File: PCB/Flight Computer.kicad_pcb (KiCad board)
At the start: 6 copper layers, 30 x 60 mm, 80 parts, among them J501 Conn_02x03_Counter_Clockwise, J502 USB_C_Receptacle_USB2.0_16P, J503 Screw_Terminal_01x06, J504 Screw_Terminal_01x04, J505 Conn_01x04, J506 Conn_02x03_Counter_Clockwise, J507 Conn_01x05, J601 Conn_Coaxial, U201 LM1117MP-3.3, U301 W25Q128JVS, U302 STM32F446RETx, U401 MMC5633NJL, U402 LSM6DSV320, U403 MS5607-02BA, U404 SAM-M8Q, U601 RFM95W-915S2, Y301 Resonator

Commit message: Renamed nets from pryo to pyro cause I can't spell
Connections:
- net /Pryo1 renamed /Pyro1
- net /Pryo1_Cont renamed /Pyro1_Cont
- net /Pryo1_Trigger renamed /Pyro1_Trigger
- net /Pryo2 renamed /Pyro2
- net /Pryo2_Cont renamed /Pyro2_Cont
- net /Pryo2_Trigger renamed /Pyro2_Trigger
- net /Pryo3 renamed /Pyro3
- net /Pryo3_Cont renamed /Pyro3_Cont
- net /Pryo3_Trigger renamed /Pyro3_Trigger
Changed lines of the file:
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@@
 	(net 11 "/NRST")
 	(net 12 "/SWCLK")
-	(net 13 "/Pryo3")
+	(net 13 "/Pyro3")
 	(net 14 "/USB_DP_N")
 	(net 15 "/USB_DP_P")
 	(net 16 "Pyro_Power")
-	(net 17 "/Pryo1")
-	(net 18 "/Pryo2")
+	(net 17 "/Pyro1")
+	(net 18 "/Pyro2")
 	(net 19 "/I2C_SDA")
 	(net 20 "/I2C_SCL")
@@
 	(net 28 "/Servo1")
 	(net 29 "Net-(J601-In)")
-	(net 30 "/Pryo1_Cont")
-	(net 31 "/Pryo2_Cont")
-	(net 32 "/Pryo3_Cont")
+	(net 30 "/Pyro1_Cont")
+	(net 31 "/Pyro2_Cont")
+	(net 32 "/Pyro3_Cont")
 	(net 33 "/MCU/OSC_OUT")
 	(net 34 "/{slash}GPS_RESET")
@@
 	(net 37 "/Armed")
 	(net 38 "Net-(U701A-G)")
-	(net 39 "/Pryo1_Trigger")
+	(net 39 "/Pyro1_Trigger")
 	(net 40 "Net-(U702B-G)")
-	(net 41 "/Pryo2_Trigger")
+	(net 41 "/Pyro2_Trigger")
 	(net 42 "Net-(U702A-G)")
 	(net 43 "Net-(U703B-G)")
 	(net 44 "Net-(U703A-G)")
-	(net 45 "/Pryo3_Trigger")
+	(net 45 "/Pyro3_Trigger")
 	(net 46 "/MCU/FLASH_CS")
 	(net 47 "/MCU/{slash}FLASH_WP")
@@
 			(layers "F.Cu" "F.Mask" "F.Paste")
 			(roundrect_rratio 0.25)
-			(net 31 "/Pryo2_Cont")
+			(net 31 "/Pyro2_Cont")
 			(pintype "passive")
 		)
@@
 			(layers "*.Cu" "*.Mask")
 			(remove_unused_layers no)
-			(net 13 "/Pryo3")
+			(net 13 "/Pyro3")
 			(pinfunction "Pin_2")
 			(pintype "passive")
@@
 			(layers "F.Cu" "F.Mask" "F.Paste")
 			(roundrect_rratio 0.25)
-			(net 41 "/Pryo2_Trigger")
+			(net 41 "/Pyro2_Trigger")
 			(pintype "passive")
 		)
@@
 			(size 0.2992 0.6298)
 			(layers "F.Cu" "F.Mask" "F.Paste")
-			(net 18 "/Pryo2")
+			(net 18 "/Pyro2")
 			(pinfunction "D")
 			(pintype "passive")
@@
 			(size 0.9906 0.7112)
 			(layers "F.Cu" "F.Mask" "F.Paste")
-			(net 18 "/Pryo2")
+			(net 18 "/Pyro2")
 			(pinfunction "D")
 			(pintype "passive")
@@
 			(layers "*.Cu" "*.Mask")
 			(remove_unused_layers no)
-			(net 17 "/Pryo1")
+			(net 17 "/Pyro1")
 			(pinfunction "Pin_3")
 			(pintype "passive")
@@
 			(layers "*.Cu" "*.Mask")
 			(remove_unused_layers no)
-			(net 18 "/Pryo2")
+			(net 18 "/Pyro2")
 			(pinfunction "Pin_5")
 			(pintype "passive")
@@
 			(layers "F.Cu" "F.Mask" "F.Paste")
 			(roundrect_rratio 0.25)
-			(net 31 "/Pryo2_Cont")
+			(net 31 "/Pyro2_Cont")
 			(pintype "passive")
 		)
@@
 			(size 0.2992 0.6298)
 			(layers "B.Cu" "B.Mask" "B.Paste")
-			(net 17 "/Pryo1")
+			(net 17 "/Pyro1")
 			(pinfunction "D")
 			(pintype "passive")
@@
 			(size 0.9906 0.7112)
 			(layers "B.Cu" "B.Mask" "B.Paste")
-			(net 17 "/Pryo1")
+			(net 17 "/Pyro1")
 			(pinfunction "D")
 			(pintype "passive")
@@
 			(layers "B.Cu" "B.Mask" "B.Paste")
 			(roundrect_rratio 0.25)
-			(net 32 "/Pryo3_Cont")
+			(net 32 "/Pyro3_Cont")
 			(pintype "passive")
 		)
@@
 			(layers "B.Cu" "B.Mask" "B.Paste")
 			(roundrect_rratio 0.25)
-			(net 32 "/Pryo3_Cont")
+			(net 32 "/Pyro3_Cont")
 			(pintype "passive")
 		)
@@
 			(layers "B.Cu" "B.Mask" "B.Paste")
 			(roundrect_rratio 0.25)
-			(net 39 "/Pryo1_Trigger")
+			(net 39 "/Pyro1_Trigger")
 			(pintype "passive")
 		)
@@
 			(layers "B.Cu" "B.Mask" "B.Paste")
 			(roundrect_rratio 0.25)
-			(net 13 "/Pryo3")
+			(net 13 "/Pyro3")
 			(pintype "passive")
 		)
@@
 			(layers "B.Cu" "B.Mask" "B.Paste")
 			(roundrect_rratio 0.25)
-			(net 18 "/Pryo2")
+			(net 18 "/Pyro2")
 			(pintype "passive")
 		)
@@
 			(layers "B.Cu" "B.Mask" "B.Paste")
 			(roundrect_rratio 0.25)
-			(net 30 "/Pryo1_Cont")
+			(net 30 "/Pyro1_Cont")
 			(pintype "passive")
 		)
@@
 			(layers "B.Cu" "B.Mask" "B.Paste")
 			(roundrect_rratio 0.25)
-			(net 45 "/Pryo3_Trigger")
+			(net 45 "/Pyro3_Trigger")
 			(pintype "passive")
 		)
@@
 			(layers "B.Cu" "B.Mask" "B.Paste")
 			(roundrect_rratio 0.25)
-			(net 17 "/Pryo1")
+			(net 17 "/Pyro1")
 			(pintype "passive")
 		)
@@
 			(layers "B.Cu" "B.Mask" "B.Paste")
 			(roundrect_rratio 0.25)
-			(net 45 "/Pryo3_Trigger")
+			(net 45 "/Pyro3_Trigger")
 			(pinfunction "PC1")
 			(pintype "bidirectional")
@@
 			(layers "B.Cu" "B.Mask" "B.Paste")
 			(roundrect_rratio 0.25)
-			(net 41 "/Pryo2_Trigger")
+			(net 41 "/Pyro2_Trigger")
 			(pinfunction "PC2")
 			(pintype "bidirectional")
@@
 			(layers "B.Cu" "B.Mask" "B.Paste")
 			(roundrect_rratio 0.25)
-			(net 39 "/Pryo1_Trigger")
+			(net 39 "/Pyro1_Trigger")
 			(pinfunction "PC3")
 			(pintype "bidirectional")
@@
 			(layers "B.Cu" "B.Mask" "B.Paste")
 			(roundrect_rratio 0.25)
-			(net 31 "/Pryo2_Cont")
+			(net 31 "/Pyro2_Cont")
 			(pinfunction "PA0")
 			(pintype "bidirectional")
@@
 			(layers "B.Cu" "B.Mask" "B.Paste")
 			(roundrect_rratio 0.25)
-			(net 30 "/Pryo1_Cont")
+			(net 30 "/Pyro1_Cont")
 			(pinfunction "PA1")
 			(pintype "bidirectional")
@@
 			(layers "B.Cu" "B.Mask" "B.Paste")
 			(roundrect_rratio 0.25)
-			(net 32 "/Pryo3_Cont")
+			(net 32 "/Pyro3_Cont")
 			(pinfunction "PA3")
 			(pintype "bidirectional")
@@
 			(size 0.2992 0.6298)
 			(layers "B.Cu" "B.Mask" "B.Paste")
-			(net 13 "/Pryo3")
+			(net 13 "/Pyro3")
 			(pinfunction "D")
 			(pintype "passive")
@@
 			(size 0.9906 0.7112)
 			(layers "B.Cu" "B.Mask" "B.Paste")
-			(net 13 "/Pryo3")
+			(net 13 "/Pyro3")
 			(pinfunction "D")
 			(pintype "passive")
@@
 			(layers "B.Cu" "B.Mask" "B.Paste")
 			(roundrect_rratio 0.25)
-			(net 30 "/Pryo1_Cont")
+			(net 30 "/Pyro1_Cont")
 			(pintype "passive")
 		)

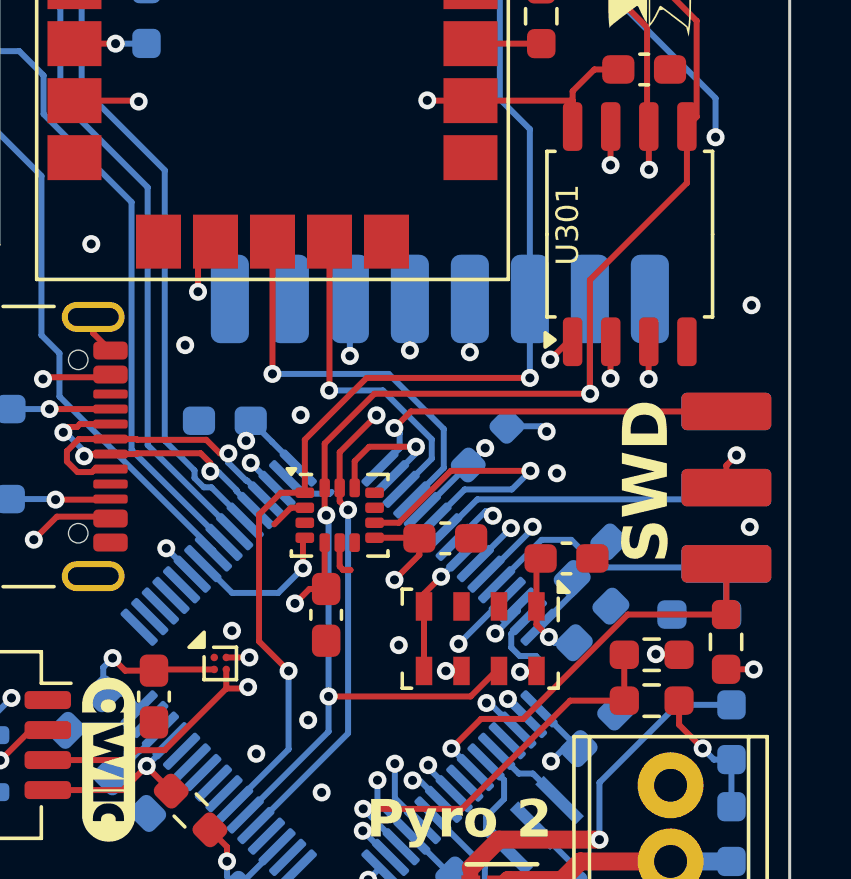
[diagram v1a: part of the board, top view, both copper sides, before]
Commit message: Flipped MOSI and MISO on the IMU
Updated all output files for the PCB
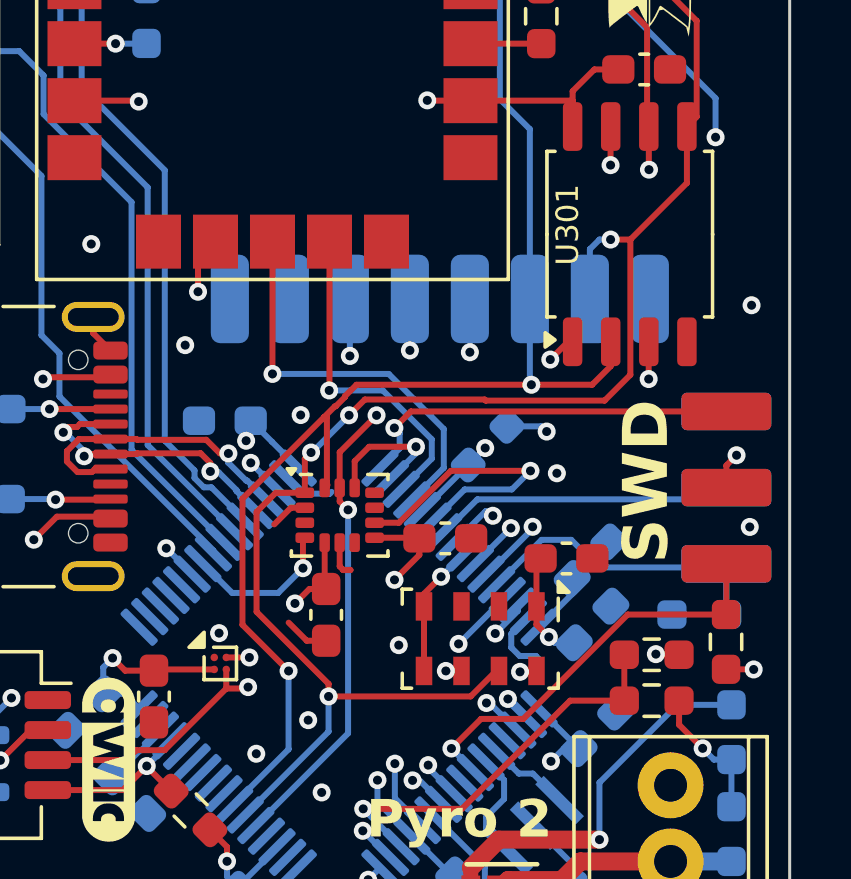
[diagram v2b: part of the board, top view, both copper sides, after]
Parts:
- R701, R708, R713: value 1k -> 10k
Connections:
- U402 pad 1: /SPI_MOSI -> /SPI_MISO
- U402 pad 14: /SPI_MISO -> /SPI_MOSI
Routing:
- net /SPI_MISO: track 59.6 -> 62.5 mm, vias 3 -> 4
- net /SPI_MOSI: track 56.4 -> 59.1 mm, vias 4 -> 3
- net GND: track 13.9 -> 15.4 mm

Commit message: Cleaned up schematic Change from SPI and I2C to busses
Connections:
- U601 pad 2: /SPI_MISO -> /Radio/SPI_MISO
- U601 pad 3: /SPI_MOSI -> /Radio/SPI_MOSI
- U601 pad 4: /SPI_SCK -> /Radio/SPI_SCK
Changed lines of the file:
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@@
 	(net 86 "Net-(R714-Pad2)")
 	(net 87 "/MCU/PB1")
+	(net 88 "/Radio/SPI_MISO")
+	(net 89 "/Radio/SPI_MOSI")
+	(net 90 "/Radio/SPI_SCK")
 	(footprint "Resistor_SMD:R_0603_1608Metric_Pad0.98x0.95mm_HandSolder"
 		(layer "F.Cu")
@@
 			(layers "B.Cu" "B.Mask" "B.Paste")
 			(roundrect_rratio 0.25)
-			(net 24 "/SPI_MISO")
+			(net 88 "/Radio/SPI_MISO")
 			(pinfunction "MISO")
 			(pintype "output")
@@
 			(layers "B.Cu" "B.Mask" "B.Paste")
 			(roundrect_rratio 0.25)
-			(net 22 "/SPI_MOSI")
+			(net 89 "/Radio/SPI_MOSI")
 			(pinfunction "MOSI")
 			(pintype "input")
@@
 			(layers "B.Cu" "B.Mask" "B.Paste")
 			(roundrect_rratio 0.25)
-			(net 21 "/SPI_SCK")
+			(net 90 "/Radio/SPI_SCK")
 			(pinfunction "SCK")
 			(pintype "input")

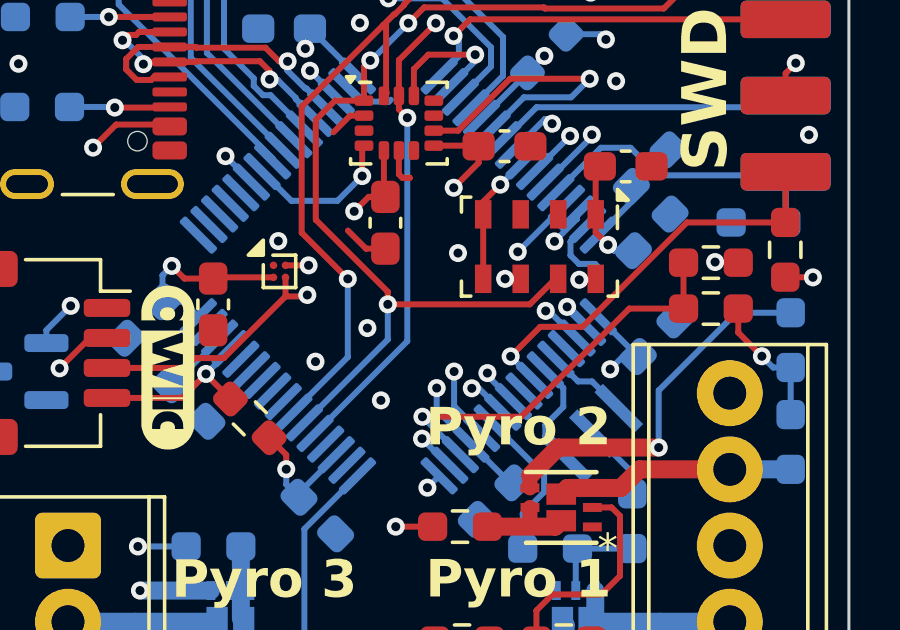
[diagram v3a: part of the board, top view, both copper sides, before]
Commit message: Update Barometer SPI connection
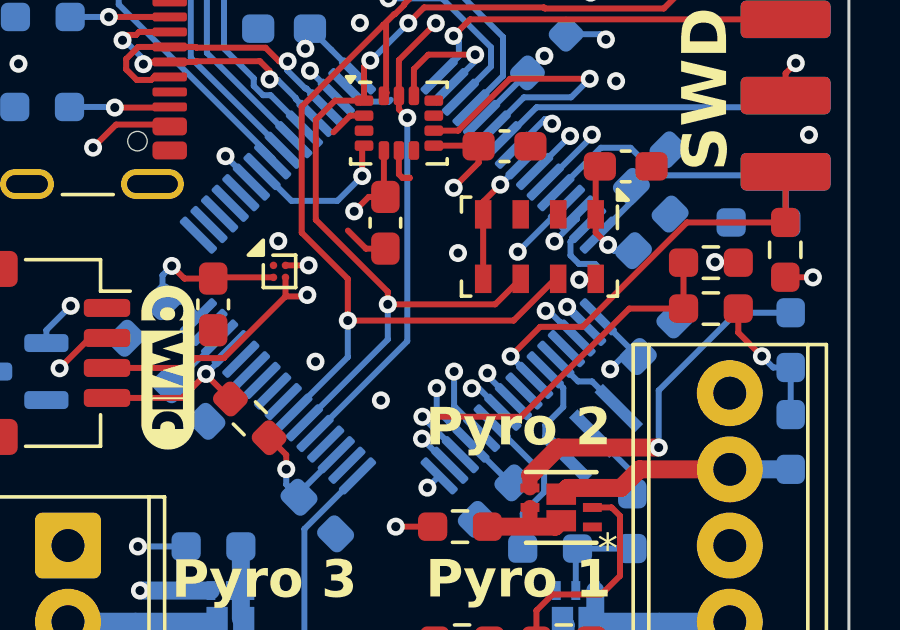
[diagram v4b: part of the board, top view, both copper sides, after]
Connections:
- U403 pad 6: /SPI_MOSI -> /SPI_MISO
- U403 pad 7: /SPI_MISO -> /SPI_MOSI
- U601 pad 2: /Radio/SPI_MISO -> /SPI_MISO
- U601 pad 3: /Radio/SPI_MOSI -> /SPI_MOSI
- U601 pad 4: /Radio/SPI_SCK -> /SPI_SCK
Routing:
- net /SPI_MOSI: track 59.1 -> 61.0 mm, vias 3 -> 2
- net /SPI_MISO: track 62.5 -> 61.3 mm
- net GND: vias 28 -> 27
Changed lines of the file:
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@@
 	(net 86 "Net-(R714-Pad2)")
 	(net 87 "/MCU/PB1")
-	(net 88 "/Radio/SPI_MISO")
-	(net 89 "/Radio/SPI_MOSI")
-	(net 90 "/Radio/SPI_SCK")
 	(footprint "Resistor_SMD:R_0603_1608Metric_Pad0.98x0.95mm_HandSolder"
 		(layer "F.Cu")
@@
 			(size 0.95 0.55)
 			(layers "F.Cu" "F.Mask" "F.Paste")
-			(net 22 "/SPI_MOSI")
+			(net 24 "/SPI_MISO")
 			(pinfunction "SDO")
 			(pintype "output")
@@
 			(size 0.95 0.55)
 			(layers "F.Cu" "F.Mask" "F.Paste")
-			(net 24 "/SPI_MISO")
+			(net 22 "/SPI_MOSI")
 			(pinfunction "SDI/SDA")
 			(pintype "bidirectional")
@@
 			(layers "B.Cu" "B.Mask" "B.Paste")
 			(roundrect_rratio 0.25)
-			(net 88 "/Radio/SPI_MISO")
+			(net 24 "/SPI_MISO")
 			(pinfunction "MISO")
 			(pintype "output")
@@
 			(layers "B.Cu" "B.Mask" "B.Paste")
 			(roundrect_rratio 0.25)
-			(net 89 "/Radio/SPI_MOSI")
+			(net 22 "/SPI_MOSI")
 			(pinfunction "MOSI")
 			(pintype "input")
@@
 			(layers "B.Cu" "B.Mask" "B.Paste")
 			(roundrect_rratio 0.25)
-			(net 90 "/Radio/SPI_SCK")
+			(net 21 "/SPI_SCK")
 			(pinfunction "SCK")
 			(pintype "input")
@@
 	)
 	(via
-		(at 111.62 89.33)
-		(size 0.6)
-		(drill 0.3)
-		(layers "F.Cu" "B.Cu")
-		(free yes)
-		(net 1)
-	)
-	(via
 		(at 114.51 90.78)
 		(size 0.6)
@@
 	)
 	(segment
-		(start 109.43 86.153)
-		(end 109.43 81.95)
+		(start 109.43 81.95)
+		(end 112.155 79.225)
 		(width 0.2)
 		(layer "F.Cu")
@@
 	)
 	(segment
-		(start 116.73 87.690001)
-		(end 116.21 87.69)
-		(width 0.2)
-		(layer "F.Cu")
-		(net 22)
-	)
-	(segment
-		(start 109.43 81.95)
-		(end 112.155 79.225)
+		(start 109.43 86.153)
+		(end 109.43 81.95)
 		(width 0.2)
 		(layer "F.Cu")
@@
 	)
 	(segment
+		(start 110.967 89.08)
+		(end 116.494807 89.08)
+		(width 0.2)
+		(layer "F.Cu")
+		(net 22)
+	)
+	(segment
+		(start 110.967 89.08)
+		(end 110.967 87.69)
+		(width 0.2)
+		(layer "F.Cu")
+		(net 22)
+	)
+	(segment
 		(start 121.705 76.7175)
 		(end 121.705 77.529999)
@@
 	)
 	(segment
+		(start 117.884806 87.690001)
+		(end 117.98 87.690001)
+		(width 0.2)
+		(layer "F.Cu")
+		(net 22)
+	)
+	(segment
 		(start 112.17 81.5875)
 		(end 112.243811 81.513689)
@@
 		(net 22)
 	)
-	(via
-		(at 116.21 87.69)
-		(size 0.6)
-		(drill 0.3)
-		(layers "F.Cu" "B.Cu")
+	(segment
+		(start 116.494807 89.08)
+		(end 117.884806 87.690001)
+		(width 0.2)
+		(layer "F.Cu")
 		(net 22)
 	)
 	(via
-		(at 110.967 87.69)
+		(at 110.967 89.08)
 		(size 0.6)
 		(drill 0.3)
@@
 	)
 	(segment
-		(start 110.967 90.299813)
-		(end 109.168551 92.098262)
-		(width 0.2)
-		(layer "B.Cu")
-		(net 22)
-	)
-	(segment
-		(start 110.967 87.69)
+		(start 110.967 89.08)
 		(end 110.967 90.299813)
 		(width 0.2)
@@
 	)
 	(segment
-		(start 110.967 87.69)
-		(end 116.21 87.69)
+		(start 110.967 90.299813)
+		(end 109.168551 92.098262)
 		(width 0.2)
-		(layer "In2.Cu")
+		(layer "B.Cu")
 		(net 22)
 	)
@@
 	)
 	(segment
-		(start 117.035347 88.54)
-		(end 117.885346 87.690001)
-		(width 0.2)
-		(layer "F.Cu")
-		(net 24)
-	)
-	(segment
 		(start 124.245 71.425)
 		(end 124.245 69.5425)
@@
 	)
 	(segment
+		(start 112.299749 88.54)
+		(end 115.880001 88.54)
+		(width 0.2)
+		(layer "F.Cu")
+		(net 24)
+	)
+	(segment
 		(start 124.245 69.5425)
 		(end 124.569999 69.217501)
@@
 	)
 	(segment
-		(start 117.885346 87.690001)
-		(end 117.98 87.690001)
-		(width 0.2)
-		(layer "F.Cu")
-		(net 24)
-	)
-	(segment
-		(start 112.299749 88.54)
-		(end 117.035347 88.54)
-		(width 0.2)
-		(layer "F.Cu")
-		(net 24)
-	)
-	(segment
 		(start 112.983751 79.168246)
 		(end 113.509997 78.642)
@@
 		(width 0.2)
 		(layer "F.Cu")
+		(net 24)
+	)
+	(segment
+		(start 115.880001 88.54)
+		(end 116.73 87.690001)
+		(width 0.2)
+		(layer "F.Cu")
